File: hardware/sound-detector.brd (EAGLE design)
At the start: 43.2 x 22.9 mm, 36 parts, among them U1 LMV324

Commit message: Changing resistor value convention.
R12 changed from 3k3 to 3.3k.
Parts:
- R12: value 3k3 -> 3.3k
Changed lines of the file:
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@@
 <layer number="43" name="vRestrict" color="2" fill="10" visible="no" active="yes"/>
 <layer number="44" name="Drills" color="7" fill="1" visible="no" active="yes"/>
-<layer number="45" name="Holes" color="7" fill="1" visible="no" active="yes"/>
+<layer number="45" name="Holes" color="7" fill="1" visible="yes" active="yes"/>
 <layer number="46" name="Milling" color="3" fill="1" visible="no" active="yes"/>
 <layer number="47" name="Measures" color="7" fill="1" visible="no" active="yes"/>
 <layer number="48" name="Document" color="7" fill="1" visible="no" active="yes"/>
-<layer number="49" name="Reference" color="7" fill="1" visible="no" active="yes"/>
+<layer number="49" name="Reference" color="7" fill="1" visible="yes" active="yes"/>
 <layer number="50" name="dxf" color="7" fill="1" visible="no" active="no"/>
 <layer number="51" name="tDocu" color="6" fill="1" visible="yes" active="yes"/>
@@
 <attribute name="PROD_ID" value="RES-07828" x="24.13" y="19.05" size="1.778" layer="27" font="vector" ratio="15" rot="R90" display="off"/>
 </element>
-<element name="R12" library="SparkFun-Resistors" package="0603-RES" value="3k3" x="21.59" y="19.05" rot="R270">
+<element name="R12" library="SparkFun-Resistors" package="0603-RES" value="3.3k" x="21.59" y="19.05" rot="R270">
 <attribute name="PROD_ID" value="RES-07851" x="21.59" y="19.05" size="1.778" layer="27" rot="R270" display="off"/>
 </element>

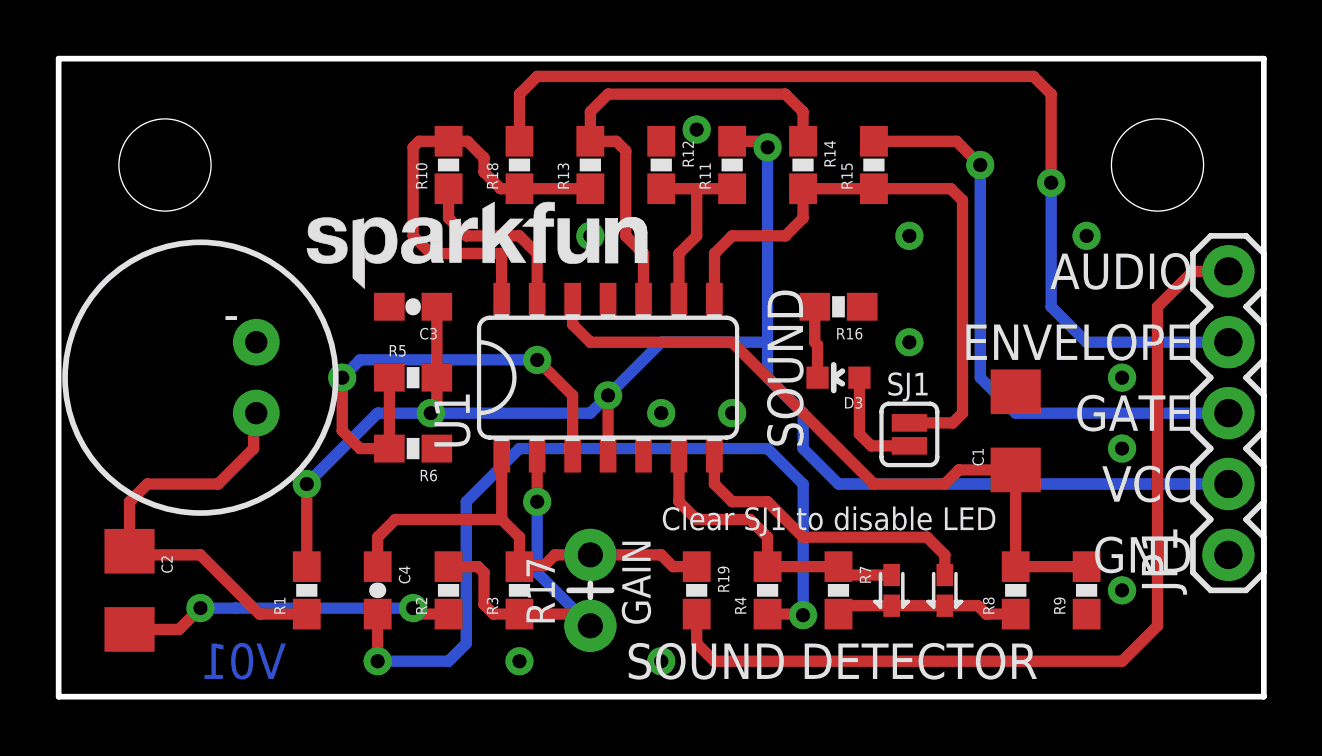
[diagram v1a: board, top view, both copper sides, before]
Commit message: Changes based on green board review
-All text to vector
-fixed diode footprint to diodes.inc recommendations
--Added legend text for gain set resistors
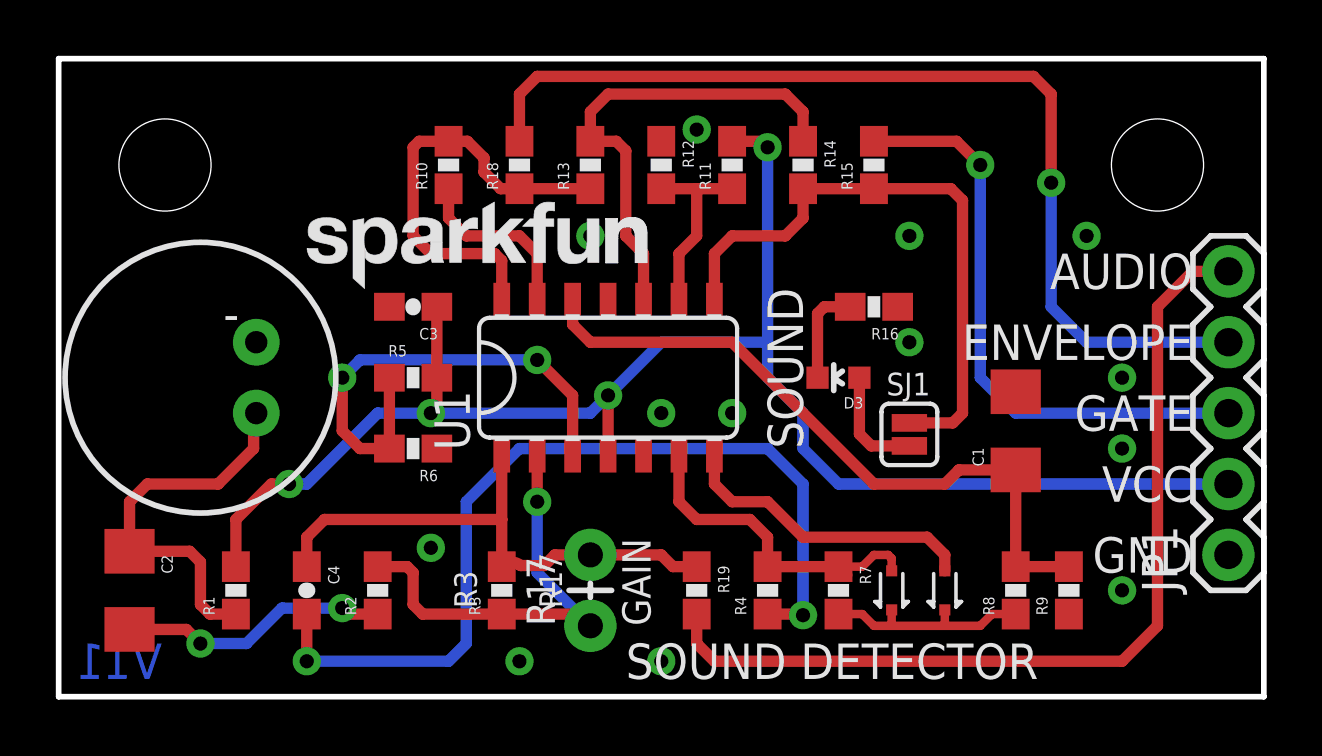
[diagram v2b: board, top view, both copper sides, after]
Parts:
- moved R1 2.54 mm to (6.35, 3.81)
- moved R2 2.54 mm to (11.4, 3.81)
- moved C4 2.54 mm to (8.89, 3.81)
- moved R16 1.27 mm to (29.2, 14.0)
- moved R3 0.64 mm to (15.9, 3.81)
- moved R9 0.63 mm to (36.2, 3.81)
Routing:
- net N$: track 16.7 -> 19.6 mm
- net N$6: track 29.6 -> 32.2 mm
- net N$4: track 13.5 -> 16.0 mm
- net N$5: track 11.8 -> 9.71 mm
- net VCC: track 56.1 -> 57.9 mm
- net N$1: track 15.6 -> 14.0 mm
- net N$9: track 6.60 -> 8.14 mm
- net N$7: track 11.0 -> 12.1 mm
- net N$3: track 2.58 -> 3.57 mm
- net N$10: track 25.4 -> 24.7 mm
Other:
- board text added: "R17"
- board text added: "R3"
- board text added: "V11"
- board text removed: "V01"

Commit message: Ready for reds
Changed after group review:
-net width of schem
-Vector text
-IC naming
-Correct logos
-Minor electrical cleanup
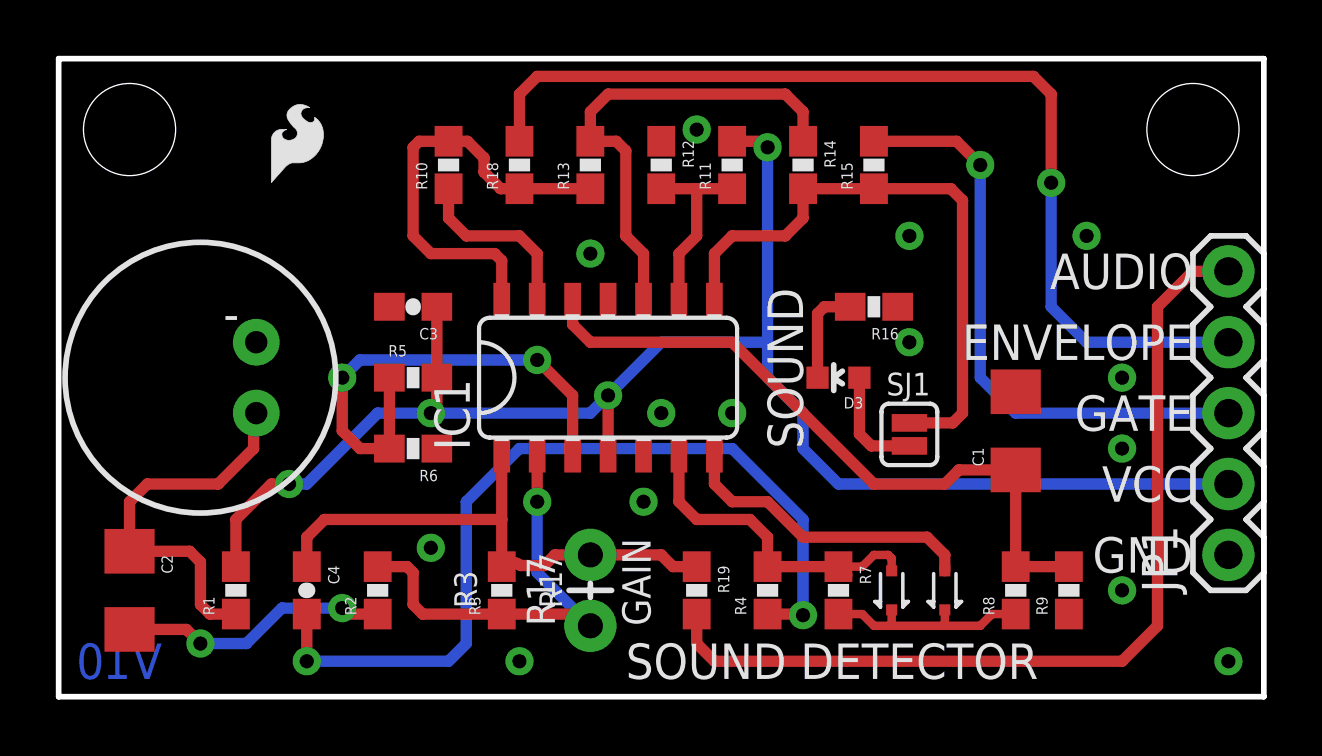
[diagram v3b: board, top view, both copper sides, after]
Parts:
- LOGO2: value LOGO-SFENEW -> LOGO-SFENW2; device SparkFun-Aesthetics:SFE-NEW-WEBLOGO -> SparkFun-Aesthetics:SFE-NEW-WEB
- LOGO3: value LOGO-SFENW2 -> LOGO-SFESK; device SparkFun-Aesthetics:SFE-NEW-WEB -> SparkFun-Aesthetics:SFE-LOGO-FLAME
- moved LOGO2 8.13 mm to (20.3, 17.8)
- moved LOGO3 4.02 mm to (7.62, 18.4)
- moved STANDOFF2 1.80 mm to (40.6, 20.3)
- moved STANDOFF1 1.80 mm to (2.54, 20.3)
- renumbered U1 to IC1
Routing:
- net N$6: track 32.2 -> 31.4 mm
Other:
- board text added: "V10"
- board text removed: "V11"
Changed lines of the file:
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@@
 <layer number="49" name="Reference" color="7" fill="1" visible="yes" active="yes"/>
 <layer number="50" name="dxf" color="7" fill="1" visible="no" active="no"/>
-<layer number="51" name="tDocu" color="6" fill="1" visible="yes" active="yes"/>
+<layer number="51" name="tDocu" color="6" fill="1" visible="no" active="yes"/>
 <layer number="52" name="bDocu" color="7" fill="1" visible="no" active="yes"/>
 <layer number="53" name="tGND_GNDA" color="7" fill="9" visible="no" active="no"/>
@@
 <text x="40.64" y="15.24" size="1.27" layer="22" font="vector" ratio="15" rot="MR180" align="center-right">AUDIO</text>
 <text x="27.94" y="8.509" size="0.8128" layer="22" font="vector" ratio="15" rot="MR0">Clear SJ1 to disable LED</text>
-<text x="0.635" y="1.27" size="1.27" layer="16" font="vector" ratio="15" rot="MR0" align="center-right">V11</text>
+<text x="0.635" y="1.27" size="1.27" layer="16" font="vector" ratio="15" rot="MR0" align="center-right">V10</text>
 <text x="20.32" y="0.635" size="1.27" layer="21" font="vector" ratio="15">SOUND DETECTOR</text>
-<text x="25.4" y="11.43" size="1.27" layer="22" font="vector" ratio="15" rot="MR0">SOUND DETECTOR</text>
+<text x="22.86" y="16.51" size="1.27" layer="22" font="vector" ratio="15" rot="MR0">SOUND DETECTOR</text>
 <text x="14.986" y="3.175" size="0.8128" layer="21" font="vector" ratio="15" rot="R90">R3</text>
 <text x="18.034" y="3.175" size="0.8128" layer="21" font="vector" ratio="15" rot="R90">R17</text>
@@
 <attribute name="PROD_ID" value="COMP-08856" x="5.08" y="11.43" size="1.778" layer="27" font="vector" ratio="15" rot="R180" display="off"/>
 </element>
-<element name="U1" library="SparkFun-AnalogIC" package="SO014" value="LMV324" x="19.05" y="11.43">
+<element name="IC1" library="SparkFun-AnalogIC" package="SO014" value="LMV324" x="19.05" y="11.43">
 <attribute name="PROD_ID" value="IC-08227" x="19.05" y="11.43" size="1.778" layer="27" font="vector" ratio="15" display="off"/>
 </element>
@@
 </element>
 <element name="LOGO1" library="SparkFun-Aesthetics" package="OSHW-LOGO-M" value="OSHW-LOGOM" x="3.81" y="11.43" rot="MR270"/>
-<element name="LOGO2" library="SparkFun-Aesthetics" package="SFE-NEW-WEBLOGO" value="LOGO-SFENEW" x="26.67" y="12.7" rot="MR0"/>
-<element name="LOGO3" library="SparkFun-Aesthetics" package="SFE-NEW-WEB" value="LOGO-SFENW2" x="8.89" y="14.605"/>
+<element name="LOGO2" library="SparkFun-Aesthetics" package="SFE-NEW-WEB" value="LOGO-SFENW2" x="20.32" y="17.78" rot="MR0"/>
+<element name="LOGO3" library="SparkFun-Aesthetics" package="SFE-LOGO-FLAME" value="LOGO-SFESK" x="7.62" y="18.415"/>
 <element name="C4" library="SparkFun-Capacitors" package="0603-CAP" value="1.0uF" x="8.89" y="3.81" rot="R270">
 <attribute name="PROD_ID" value="CAP-00868" x="8.89" y="3.81" size="1.778" layer="27" font="vector" ratio="15" rot="R270" display="off"/>
@@
 <attribute name="PROD_ID" value="RES-07863" x="22.86" y="3.81" size="1.778" layer="27" font="vector" ratio="15" rot="R270" display="off"/>
 </element>
-<element name="STANDOFF1" library="SparkFun-Electromechanical" package="STAND-OFF" value="STAND-OFF" x="3.81" y="19.05"/>
-<element name="STANDOFF2" library="SparkFun-Electromechanical" package="STAND-OFF" value="STAND-OFF" x="39.37" y="19.05"/>
+<element name="STANDOFF1" library="SparkFun-Electromechanical" package="STAND-OFF" value="STAND-OFF" x="2.54" y="20.32"/>
+<element name="STANDOFF2" library="SparkFun-Electromechanical" package="STAND-OFF" value="STAND-OFF" x="40.64" y="20.32"/>
 </elements>
 <signals>
 <signal name="GND">
 <contactref element="R6" pad="1"/>
-<contactref element="U1" pad="11"/>
+<contactref element="IC1" pad="11"/>
 <contactref element="C1" pad="2"/>
 <contactref element="R9" pad="1"/>
-<contactref element="U1" pad="5"/>
+<contactref element="IC1" pad="5"/>
 <contactref element="R12" pad="1"/>
 <contactref element="JP1" pad="1"/>
@@
 <contactref element="C3" pad="2"/>
 <via x="22.86" y="20.32" extent="1-16" drill="0.508"/>
-<via x="19.05" y="16.51" extent="1-16" drill="0.508"/>
+<via x="19.05" y="15.875" extent="1-16" drill="0.508"/>
 <via x="38.1" y="3.81" extent="1-16" drill="0.508"/>
 <via x="38.1" y="8.89" extent="1-16" drill="0.508"/>
@@
 <via x="24.13" y="10.16" extent="1-16" drill="0.508"/>
 <via x="21.59" y="10.16" extent="1-16" drill="0.508"/>
-<via x="21.59" y="1.27" extent="1-16" drill="0.508"/>
+<via x="41.91" y="1.27" extent="1-16" drill="0.508"/>
 <via x="16.51" y="1.27" extent="1-16" drill="0.508"/>
 <via x="30.48" y="16.51" extent="1-16" drill="0.508"/>
 <via x="30.48" y="12.7" extent="1-16" drill="0.508"/>
 <via x="13.335" y="5.334" extent="1-16" drill="0.508"/>
+<via x="20.955" y="6.985" extent="1-16" drill="0.508"/>
 </signal>
 <signal name="N$1">
@@
 <contactref element="R1" pad="2"/>
 <contactref element="R5" pad="2"/>
-<contactref element="U1" pad="4"/>
+<contactref element="IC1" pad="4"/>
 <contactref element="R11" pad="2"/>
 <contactref element="JP1" pad="2"/>
@@
 <contactref element="R5" pad="1"/>
 <contactref element="R6" pad="2"/>
-<contactref element="U1" pad="3"/>
+<contactref element="IC1" pad="3"/>
 <wire x1="11.85" y1="8.89" x2="11.85" y2="11.43" width="0.4064" layer="1"/>
 <wire x1="18.415" y1="8.63" x2="18.415" y2="10.795" width="0.4064" layer="1"/>
@@
 <contactref element="R3" pad="1"/>
 <contactref element="R2" pad="2"/>
-<contactref element="U1" pad="2"/>
+<contactref element="IC1" pad="2"/>
 <contactref element="R17" pad="P$1"/>
 <wire x1="15.875" y1="2.96" x2="18.63" y2="2.96" width="0.4064" layer="1"/>
@@
 <contactref element="C4" pad="2"/>
 <via x="26.67" y="2.921" extent="1-16" drill="0.508"/>
-<wire x1="26.67" y1="2.921" x2="26.67" y2="7.62" width="0.4064" layer="16"/>
-<wire x1="26.67" y1="7.62" x2="25.4" y2="8.89" width="0.4064" layer="16"/>
-<wire x1="25.4" y1="8.89" x2="16.51" y2="8.89" width="0.4064" layer="16"/>
+<wire x1="26.67" y1="2.921" x2="26.67" y2="6.35" width="0.4064" layer="16"/>
+<wire x1="26.67" y1="6.35" x2="24.13" y2="8.89" width="0.4064" layer="16"/>
+<wire x1="24.13" y1="8.89" x2="16.51" y2="8.89" width="0.4064" layer="16"/>
 <wire x1="16.51" y1="8.89" x2="14.605" y2="6.985" width="0.4064" layer="16"/>
 <via x="8.89" y="1.27" extent="1-16" drill="0.508"/>
@@
 <signal name="N$7">
 <contactref element="R4" pad="2"/>
-<contactref element="U1" pad="6"/>
+<contactref element="IC1" pad="6"/>
 <contactref element="D1" pad="A"/>
 <contactref element="R7" pad="1"/>
@@
 </signal>
 <signal name="N$8">
-<contactref element="U1" pad="7"/>
+<contactref element="IC1" pad="7"/>
 <contactref element="D2" pad="A"/>
 <wire x1="23.495" y1="8.63" x2="23.495" y2="7.62" width="0.4064" layer="1"/>
@@
 <signal name="N$10">
 <contactref element="R8" pad="2"/>
-<contactref element="U1" pad="12"/>
+<contactref element="IC1" pad="12"/>
 <contactref element="R9" pad="2"/>
 <contactref element="C1" pad="1"/>
@@
 </signal>
 <signal name="N$11">
-<contactref element="U1" pad="13"/>
+<contactref element="IC1" pad="13"/>
 <contactref element="R10" pad="1"/>
 <wire x1="13.97" y1="18.2" x2="13.97" y2="17.145" width="0.4064" layer="1"/>
@@
 <signal name="AMPENV">
 <contactref element="R10" pad="2"/>
-<contactref element="U1" pad="14"/>
+<contactref element="IC1" pad="14"/>
 <contactref element="R13" pad="1"/>
 <contactref element="R18" pad="1"/>
@@
 <contactref element="R11" pad="1"/>
 <contactref element="R12" pad="2"/>
-<contactref element="U1" pad="9"/>
+<contactref element="IC1" pad="9"/>
 <wire x1="21.59" y1="18.2" x2="22.86" y2="18.2" width="0.4064" layer="1"/>
 <wire x1="22.86" y1="18.2" x2="24.13" y2="18.2" width="0.4064" layer="1"/>
@@
 <contactref element="R13" pad="2"/>
 <contactref element="R14" pad="1"/>
-<contactref element="U1" pad="10"/>
+<contactref element="IC1" pad="10"/>
 <wire x1="19.05" y1="19.9" x2="19.05" y2="20.955" width="0.4064" layer="1"/>
 <wire x1="19.05" y1="20.955" x2="19.685" y2="21.59" width="0.4064" layer="1"/>
@@
 <signal name="N$17">
 <contactref element="R14" pad="2"/>
-<contactref element="U1" pad="8"/>
+<contactref element="IC1" pad="8"/>
 <contactref element="R15" pad="1"/>
 <contactref element="SJ1" pad="2"/>
@@
 </signal>
 <signal name="N$">
-<contactref element="U1" pad="1"/>
+<contactref element="IC1" pad="1"/>
 <contactref element="R3" pad="2"/>
 <contactref element="C4" pad="1"/>
